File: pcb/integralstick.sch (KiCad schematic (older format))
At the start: 1 part, among them J2 CONN_INTEGRALSTICK_MCU_DEVICE

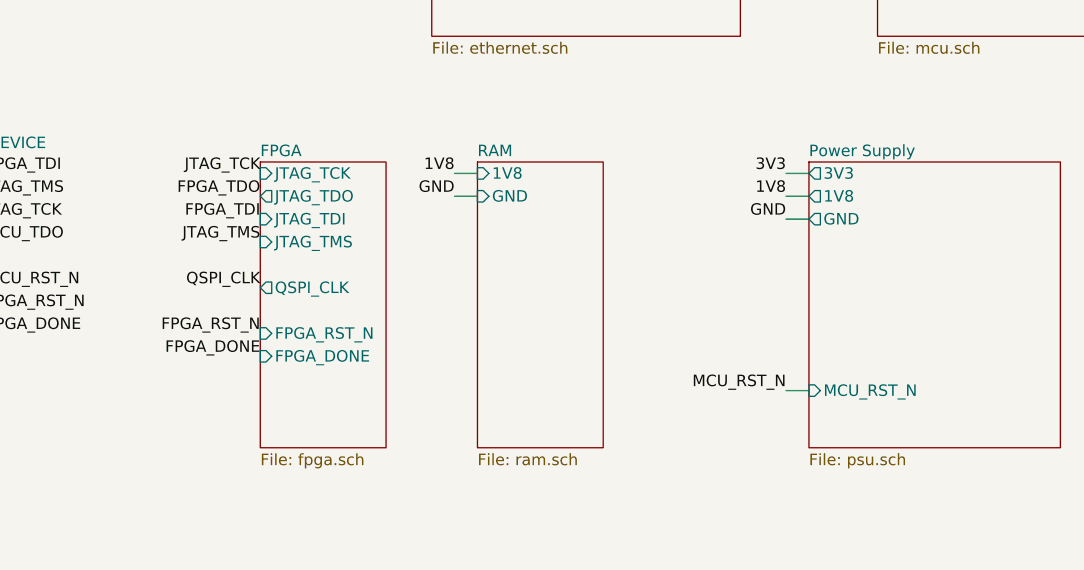
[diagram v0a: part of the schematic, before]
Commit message: Finished initial schematic. Pin assignments will likely change during routing. Ready for test point insertion and signoff review.
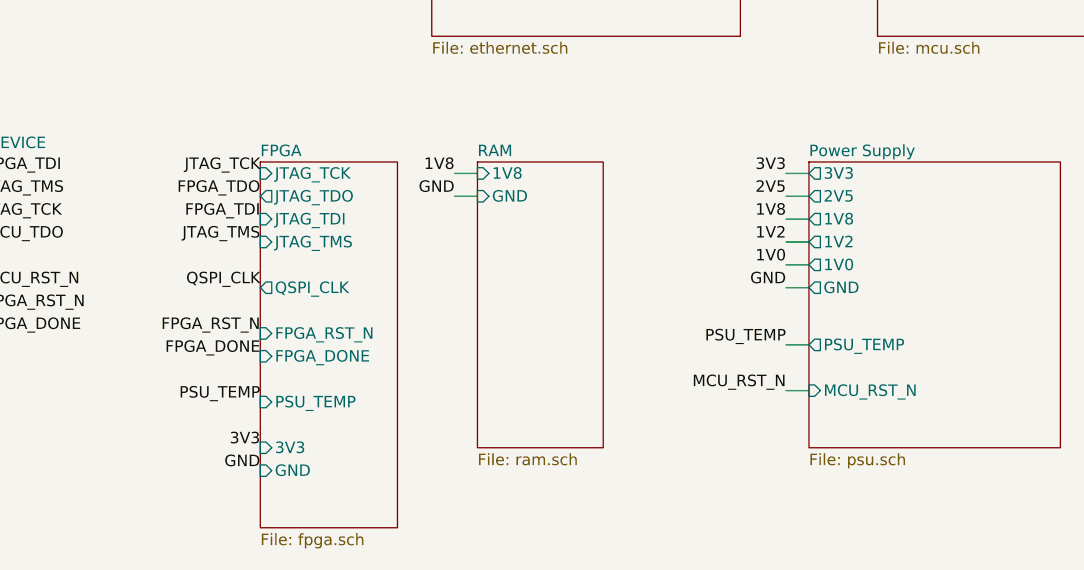
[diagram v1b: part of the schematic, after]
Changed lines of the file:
@@
 $Descr A4 11693 8268
 encoding utf-8
-Sheet 1 7
+Sheet 1 8
 Title "INTEGRALSTICK Compute Module"
-Date "2018-11-06"
+Date "2018-11-07"
 Rev "0.1"
 Comp "Andrew D. Zonenberg"
@@
 F1 "psu.sch" 50
 F2 "MCU_RST_N" I L 5100 5000 50
-F3 "GND" O L 5100 4250 50
+F3 "GND" O L 5100 4550 50
 F4 "3V3" O L 5100 4050 50
-F5 "1V8" O L 5100 4150 50
+F5 "1V8" O L 5100 4250 50
+F6 "PSU_TEMP" O L 5100 4800 50
+F7 "2V5" O L 5100 4150 50
+F8 "1V2" O L 5100 4350 50
+F9 "1V0" O L 5100 4450 50
 $EndSheet
 $Sheet
@@
 $EndSheet
 $Sheet
-S 2700 4000 550  1250
+S 2700 4000 600  1600
 U 5B6B702C
 F0 "FPGA" 50
@@
 F7 "FPGA_RST_N" I L 2700 4750 50
 F8 "FPGA_DONE" I L 2700 4850 50
+F9 "PSU_TEMP" I L 2700 5050 50
+F10 "3V3" I L 2700 5250 50
+F11 "GND" I L 2700 5350 50
 $EndSheet
 $Sheet
@@
 F23 "3V3" I L 5400 2900 50
 F24 "GND" I L 5400 3000 50
-F26 "QSPI_CLK" I R 6500 2800 50
+F25 "QSPI_CLK" I R 6500 2800 50
 $EndSheet
 Wire Wire Line
@@
 Wire Wire Line
 	5000 4050 5100 4050
-Text Label 5000 4250 2    50   ~ 0
-GND
-Wire Wire Line
-	5000 4250 5100 4250
+Text Label 5000 4550 2    50   ~ 0
+GND
+Wire Wire Line
+	5000 4550 5100 4550
 Text Label 5000 5000 2    50   ~ 0
 MCU_RST_N
 Wire Wire Line
 	5000 5000 5100 5000
-Text Label 5000 4150 2    50   ~ 0
+Text Label 5000 4250 2    50   ~ 0
 1V8
 Wire Wire Line
-	5000 4150 5100 4150
+	5000 4250 5100 4250
 Text Label 3550 4050 2    50   ~ 0
 1V8
@@
 Wire Wire Line
 	3550 4150 3650 4150
+Text Label 2700 5050 2    50   ~ 0
+PSU_TEMP
+Text Label 5000 4800 2    50   ~ 0
+PSU_TEMP
+Wire Wire Line
+	5000 4800 5100 4800
+Text Label 5000 4150 2    50   ~ 0
+2V5
+Wire Wire Line
+	5000 4150 5100 4150
+Text Label 5000 4350 2    50   ~ 0
+1V2
+Wire Wire Line
+	5000 4350 5100 4350
+Text Label 5000 4450 2    50   ~ 0
+1V0
+Wire Wire Line
+	5000 4450 5100 4450
+Text Label 2700 5250 2    50   ~ 0
+3V3
+Text Label 2700 5350 2    50   ~ 0
+GND
 $EndSCHEMATC

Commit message: Added pulldown to BOOT0 on MCU, brought it out to previously unused connector pin
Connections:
- net MCU_BOOT0: now reaches J2.12 (MCU_BOOT0)
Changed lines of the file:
@@
 F8 "1V2" O L 5100 4350 50
 F9 "1V0" O L 5100 4450 50
+F10 "MCU_BOOT0" I L 5100 5100 50
 $EndSheet
 $Sheet
@@
 Text Label 2700 5350 2    50   ~ 0
 GND
+Text Label 1500 4850 0    50   ~ 0
+MCU_BOOT0
+Wire Wire Line
+	1500 4850 1450 4850
+Text Label 5000 5100 2    50   ~ 0
+MCU_BOOT0
+Wire Wire Line
+	5000 5100 5100 5100
 $EndSCHEMATC

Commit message: Finished schematic signoff review. Fixed oscillator pinout bug, added some test points.
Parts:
- added R60: 33, symbol device:R
- added TP10, TP6, TP7, TP8, TP9: TESTPAD, symbol conn:CONN_01X01
- added TP4, TP5: TESTCLIP, symbol conn:CONN_01X01
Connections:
- net 1V0: now also TP6.1 (P1)
- net 1V2: now also TP7.1 (P1)
- net 1V8: now also TP8.1 (P1)
- net 2V5: now also TP9.1 (P1)
- net 3V3: now also TP10.1 (P1)
- net GND: now also TP4.1 (P1), TP5.1 (P1)
- net MCU_TDO: now also R60.1
- new net MCU/JTAG_TDO: R60.2
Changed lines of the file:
@@
 Sheet 1 8
 Title "INTEGRALSTICK Compute Module"
-Date "2018-11-07"
+Date "2018-11-09"
 Rev "0.1"
 Comp "Andrew D. Zonenberg"
@@
 Wire Wire Line
 	1500 4350 1450 4350
-Text Label 6550 2300 0    50   ~ 0
+Text Label 6850 2300 0    50   ~ 0
 MCU_TDO
 Wire Wire Line
@@
 Wire Wire Line
 	5000 5100 5100 5100
+$Comp
+L device:R R60
+U 1 1 5D3F25B1
+P 6700 2300
+F 0 "R60" V 6600 2300 50  0000 C CNN
+F 1 "33" V 6700 2300 50  0000 C CNN
+F 2 "" V 6630 2300 50  0001 C CNN
+F 3 "" H 6700 2300 50  0001 C CNN
+	1    6700 2300
+	0    1    1    0
+$EndComp
+$Comp
+L conn:CONN_01X01 TP4
+U 1 1 5D3FC56A
+P 10250 1050
+F 0 "TP4" H 10328 1091 50  0000 L CNN
+F 1 "TESTCLIP" H 10328 1000 50  0000 L CNN
+F 2 "" H 10250 1050 50  0001 C CNN
+F 3 "" H 10250 1050 50  0001 C CNN
+	1    10250 1050
+	1    0    0    -1
+$EndComp
+Text Label 10050 1050 2    50   ~ 0
+GND
+$Comp
+L conn:CONN_01X01 TP5
+U 1 1 5D3FCCF4
+P 10250 1250
+F 0 "TP5" H 10328 1291 50  0000 L CNN
+F 1 "TESTCLIP" H 10328 1200 50  0000 L CNN
+F 2 "" H 10250 1250 50  0001 C CNN
+F 3 "" H 10250 1250 50  0001 C CNN
+	1    10250 1250
+	1    0    0    -1
+$EndComp
+Text Label 10050 1250 2    50   ~ 0
+GND
+$Comp
+L conn:CONN_01X01 TP6
+U 1 1 5D3FE87E
+P 10250 1500
+F 0 "TP6" H 10328 1541 50  0000 L CNN
+F 1 "TESTPAD" H 10328 1450 50  0000 L CNN
+F 2 "" H 10250 1500 50  0001 C CNN
+F 3 "" H 10250 1500 50  0001 C CNN
+	1    10250 1500
+	1    0    0    -1
+$EndComp
+Text Label 10050 1500 2    50   ~ 0
+1V0
+$Comp
+L conn:CONN_01X01 TP7
+U 1 1 5D3FEB71
+P 10250 1750
+F 0 "TP7" H 10328 1791 50  0000 L CNN
+F 1 "TESTPAD" H 10328 1700 50  0000 L CNN
+F 2 "" H 10250 1750 50  0001 C CNN
+F 3 "" H 10250 1750 50  0001 C CNN
+	1    10250 1750
+	1    0    0    -1
+$EndComp
+Text Label 10050 1750 2    50   ~ 0
+1V2
+$Comp
+L conn:CONN_01X01 TP8
+U 1 1 5D4007A9
+P 10250 2000
+F 0 "TP8" H 10328 2041 50  0000 L CNN
+F 1 "TESTPAD" H 10328 1950 50  0000 L CNN
+F 2 "" H 10250 2000 50  0001 C CNN
+F 3 "" H 10250 2000 50  0001 C CNN
+	1    10250 2000
+	1    0    0    -1
+$EndComp
+Text Label 10050 2000 2    50   ~ 0
+1V8
+$Comp
+L conn:CONN_01X01 TP9
+U 1 1 5D402358
+P 10250 2250
+F 0 "TP9" H 10328 2291 50  0000 L CNN
+F 1 "TESTPAD" H 10328 2200 50  0000 L CNN
+F 2 "" H 10250 2250 50  0001 C CNN
+F 3 "" H 10250 2250 50  0001 C CNN
+	1    10250 2250
+	1    0    0    -1
+$EndComp
+Text Label 10050 2250 2    50   ~ 0
+2V5
+$Comp
+L conn:CONN_01X01 TP10
+U 1 1 5D403FC0
+P 10250 2500
+F 0 "TP10" H 10328 2541 50  0000 L CNN
+F 1 "TESTPAD" H 10328 2450 50  0000 L CNN
+F 2 "" H 10250 2500 50  0001 C CNN
+F 3 "" H 10250 2500 50  0001 C CNN
+	1    10250 2500
+	1    0    0    -1
+$EndComp
+Text Label 10050 2500 2    50   ~ 0
+3V3
 $EndSCHEMATC

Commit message: Assigned lots of footprints. Still have a few to go.
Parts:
- J2: footprint (none) -> azonenberg_pcb:CONN_SAMTEC_QTH-060-01-L-D-A
- R60: footprint (none) -> azonenberg_pcb:EIA_0402_RES_NOSILK
- TP10, TP6, TP7, TP8, TP9: footprint (none) -> azonenberg_pcb:TESTPOINT_SMT_0.5MM
- TP4, TP5: footprint (none) -> azonenberg_pcb:TESTPOINT_SMT_KEYSTONE_5016
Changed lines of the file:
@@
 F 0 "J2" H 3069 3325 50  0000 C CNN
 F 1 "CONN_INTEGRALSTICK_MCU_DEVICE" H 3069 3234 50  0000 C CNN
-F 2 "" H 2850 2050 50  0001 C CNN
+F 2 "azonenberg_pcb:CONN_SAMTEC_QTH-060-01-L-D-A" H 2850 2050 50  0001 C CNN
 F 3 "" H 2850 2050 50  0001 C CNN
 	8    2850 2050
@@
 F 0 "J2" H 1567 5975 50  0000 C CNN
 F 1 "CONN_INTEGRALSTICK_MCU_DEVICE" H 1567 5884 50  0000 C CNN
-F 2 "" H 1350 4900 50  0001 C CNN
+F 2 "azonenberg_pcb:CONN_SAMTEC_QTH-060-01-L-D-A" H 1350 4900 50  0001 C CNN
 F 3 "" H 1350 4900 50  0001 C CNN
 	2    1350 4900
@@
 F 0 "R60" V 6600 2300 50  0000 C CNN
 F 1 "33" V 6700 2300 50  0000 C CNN
-F 2 "" V 6630 2300 50  0001 C CNN
+F 2 "azonenberg_pcb:EIA_0402_RES_NOSILK" V 6630 2300 50  0001 C CNN
 F 3 "" H 6700 2300 50  0001 C CNN
 	1    6700 2300
@@
 F 0 "TP4" H 10328 1091 50  0000 L CNN
 F 1 "TESTCLIP" H 10328 1000 50  0000 L CNN
-F 2 "" H 10250 1050 50  0001 C CNN
+F 2 "azonenberg_pcb:TESTPOINT_SMT_KEYSTONE_5016" H 10250 1050 50  0001 C CNN
 F 3 "" H 10250 1050 50  0001 C CNN
 	1    10250 1050
@@
 F 0 "TP5" H 10328 1291 50  0000 L CNN
 F 1 "TESTCLIP" H 10328 1200 50  0000 L CNN
-F 2 "" H 10250 1250 50  0001 C CNN
+F 2 "azonenberg_pcb:TESTPOINT_SMT_KEYSTONE_5016" H 10250 1250 50  0001 C CNN
 F 3 "" H 10250 1250 50  0001 C CNN
 	1    10250 1250
@@
 F 0 "TP6" H 10328 1541 50  0000 L CNN
 F 1 "TESTPAD" H 10328 1450 50  0000 L CNN
-F 2 "" H 10250 1500 50  0001 C CNN
+F 2 "azonenberg_pcb:TESTPOINT_SMT_0.5MM" H 10250 1500 50  0001 C CNN
 F 3 "" H 10250 1500 50  0001 C CNN
 	1    10250 1500
@@
 F 0 "TP7" H 10328 1791 50  0000 L CNN
 F 1 "TESTPAD" H 10328 1700 50  0000 L CNN
-F 2 "" H 10250 1750 50  0001 C CNN
+F 2 "azonenberg_pcb:TESTPOINT_SMT_0.5MM" H 10250 1750 50  0001 C CNN
 F 3 "" H 10250 1750 50  0001 C CNN
 	1    10250 1750
@@
 F 0 "TP8" H 10328 2041 50  0000 L CNN
 F 1 "TESTPAD" H 10328 1950 50  0000 L CNN
-F 2 "" H 10250 2000 50  0001 C CNN
+F 2 "azonenberg_pcb:TESTPOINT_SMT_0.5MM" H 10250 2000 50  0001 C CNN
 F 3 "" H 10250 2000 50  0001 C CNN
 	1    10250 2000
@@
 F 0 "TP9" H 10328 2291 50  0000 L CNN
 F 1 "TESTPAD" H 10328 2200 50  0000 L CNN
-F 2 "" H 10250 2250 50  0001 C CNN
+F 2 "azonenberg_pcb:TESTPOINT_SMT_0.5MM" H 10250 2250 50  0001 C CNN
 F 3 "" H 10250 2250 50  0001 C CNN
 	1    10250 2250
@@
 F 0 "TP10" H 10328 2541 50  0000 L CNN
 F 1 "TESTPAD" H 10328 2450 50  0000 L CNN
-F 2 "" H 10250 2500 50  0001 C CNN
+F 2 "azonenberg_pcb:TESTPOINT_SMT_0.5MM" H 10250 2500 50  0001 C CNN
 F 3 "" H 10250 2500 50  0001 C CNN
 	1    10250 2500

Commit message: Initial routing of LVCMOS18 GPIO bus. Hooked up a few 0603 decoupling caps.
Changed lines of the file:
@@
 F9 "PSU_TEMP" I L 2700 5050 50
 F10 "3V3" I L 2700 5250 50
-F11 "GND" I L 2700 5350 50
+F11 "GND" I L 2700 5450 50
+F12 "1V8" I L 2700 5350 50
 $EndSheet
 $Sheet
@@
 Text Label 2700 5250 2    50   ~ 0
 3V3
-Text Label 2700 5350 2    50   ~ 0
+Text Label 2700 5450 2    50   ~ 0
 GND
 Text Label 1500 4850 0    50   ~ 0
@@
 Text Label 10050 2500 2    50   ~ 0
 3V3
+Text Label 2700 5350 2    50   ~ 0
+1V8
 $EndSCHEMATC
